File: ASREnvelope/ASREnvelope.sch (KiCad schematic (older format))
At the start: 47 parts

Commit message: add footprints
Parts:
- added J5: Ground, Connector_Wire:SolderWire-0.25sqmm_1x01_D0.65mm_OD2mm, symbol Connector:Conn_01x01_Female
- C1, C8: renamed from C?; footprint (none) -> Capacitor_THT:C_Disc_D3.0mm_W2.0mm_P2.50mm
- C2, C3: renamed from C?; footprint (none) -> Capacitor_THT:CP_Radial_D5.0mm_P2.00mm
- C4, C5, C6, C7: renamed from C?; footprint (none) -> Capacitor_THT:C_Rect_L10.3mm_W7.2mm_P7.50mm_MKS4
- D1, D2, D3, D4, D5, D6, D7, D8: renamed from D?; footprint (none) -> Diode_THT:D_DO-35_SOD27_P7.62mm_Horizontal
- J1, J2, J3, J4: renamed from J?; footprint (none) -> Connector_Wire:SolderWire-0.25sqmm_1x01_D0.65mm_OD2mm
- R1, R10, R11, R12, R13, R14, R15, R2, R3, R4, R5, R6, R7, R8, R9: renamed from R?; footprint (none) -> Resistor_THT:R_Axial_DIN0207_L6.3mm_D2.5mm_P7.62mm_Horizontal
- U1: renamed from U?; footprint (none) -> Package_DIP:DIP-14_W7.62mm_Socket
- U2: renamed from U?; footprint (none) -> Package_DIP:DIP-8_W7.62mm_Socket
- gave numbers to parts that had none: 4
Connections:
- net Earth: now also RV1.1, J5.1 (Pin_1); no longer RV1.3
- net at D5.1 (K): now also RV1.3; no longer RV1.1

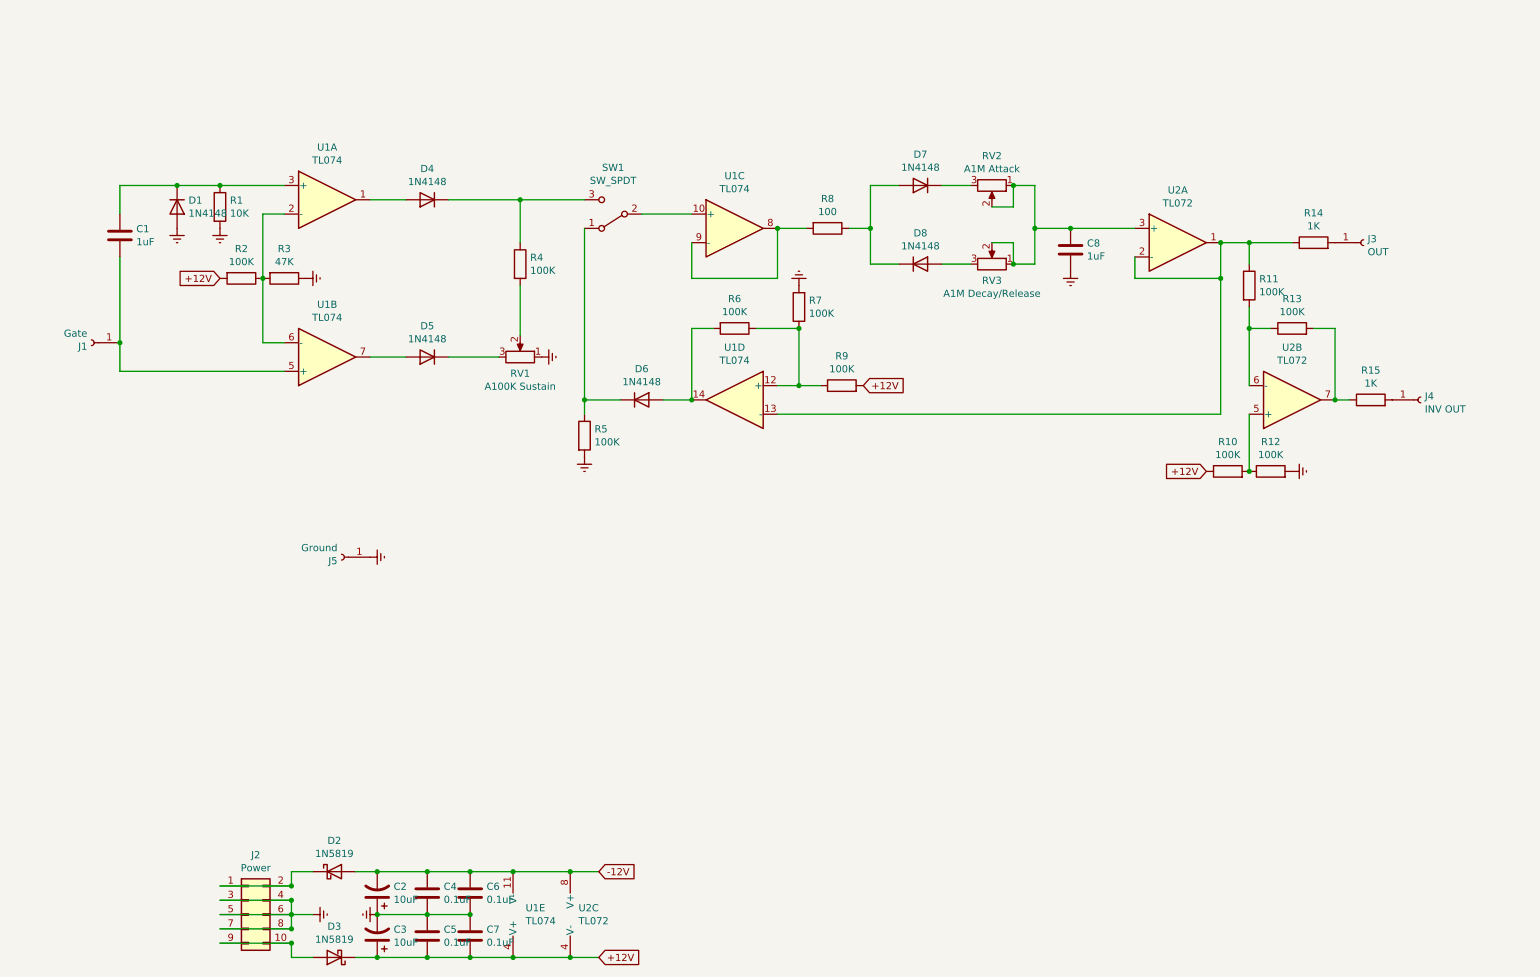
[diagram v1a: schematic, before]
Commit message: add through hole pot footprints
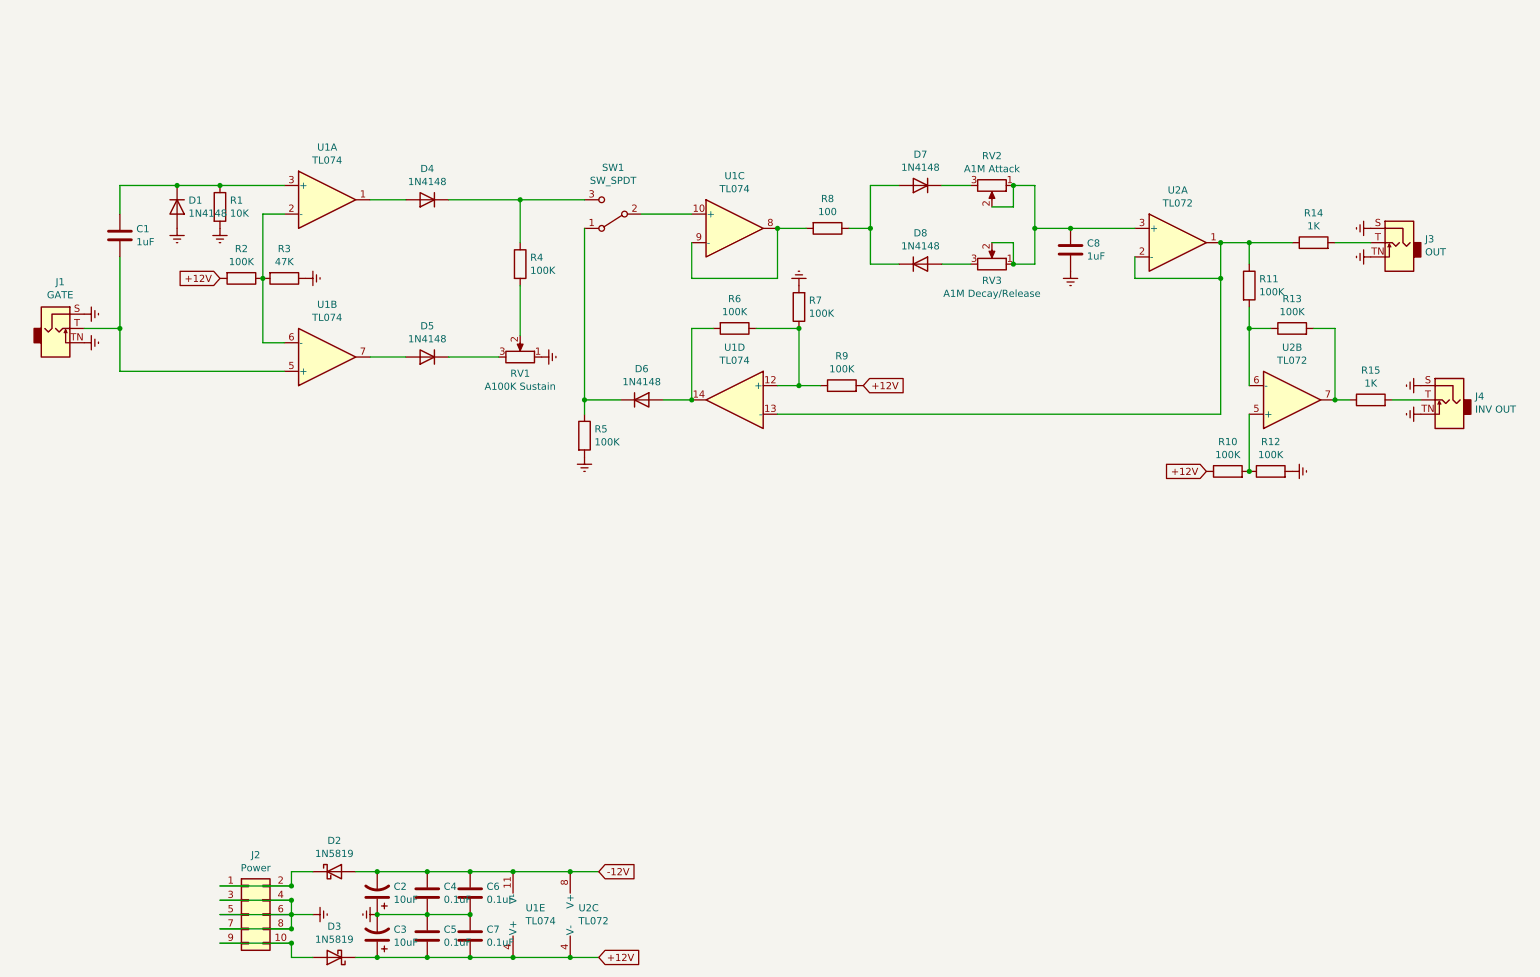
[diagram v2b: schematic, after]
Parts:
- removed J1: Gate, Connector_Wire:SolderWire-0.25sqmm_1x01_D0.65mm_OD2mm, symbol Connector:Conn_01x01_Female
- removed J3: OUT, Connector_Wire:SolderWire-0.25sqmm_1x01_D0.65mm_OD2mm, symbol Connector:Conn_01x01_Female
- removed J4: INV OUT, Connector_Wire:SolderWire-0.25sqmm_1x01_D0.65mm_OD2mm, symbol Connector:Conn_01x01_Female
- removed J5: Ground, Connector_Wire:SolderWire-0.25sqmm_1x01_D0.65mm_OD2mm, symbol Connector:Conn_01x01_Female
- added J1: GATE, Connector_Audio:Jack_3.5mm_QingPu_WQP-PJ398SM_Vertical_CircularHoles, symbol Connector:AudioJack2_SwitchT
- added J3: OUT, Connector_Audio:Jack_3.5mm_QingPu_WQP-PJ398SM_Vertical_CircularHoles, symbol Connector:AudioJack2_SwitchT
- added J4: INV OUT, Connector_Audio:Jack_3.5mm_QingPu_WQP-PJ398SM_Vertical_CircularHoles, symbol Connector:AudioJack2_SwitchT
- J2: footprint Connector_Wire:SolderWire-0.25sqmm_1x01_D0.65mm_OD2mm -> Connector_PinHeader_2.54mm:PinHeader_2x05_P2.54mm_Vertical
- RV1, RV2, RV3: footprint (none) -> Potentiometer_THT:Potentiometer_Alpha_RD901F-40-00D_Single_Vertical
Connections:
- net Earth: now also J1.S, J1.TN, J3.S, J3.TN, J4.S, J4.TN
- net at C1.2, U1.5 (+): now also J1.T
- net at R14.2: now also J3.T
- net at R15.2: now also J4.T
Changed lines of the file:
@@
 F 0 "J2" H 2300 7367 50  0000 C CNN
 F 1 "Power" H 2300 7276 50  0000 C CNN
-F 2 "Connector_Wire:SolderWire-0.25sqmm_1x01_D0.65mm_OD2mm" H 2250 6950 50  0001 C CNN
+F 2 "Connector_PinHeader_2.54mm:PinHeader_2x05_P2.54mm_Vertical" H 2250 6950 50  0001 C CNN
 F 3 "~" H 2250 6950 50  0001 C CNN
 	1    2250 6950
@@
 Wire Wire Line
 	3500 7250 3800 7250
-$Comp
-L Connector:Conn_01x01_Female J1
-U 1 1 62D5AD4C
-P 1150 2950
-F 0 "J1" H 1178 2976 50  0000 L CNN
-F 1 "Gate" H 1178 2885 50  0000 L CNN
-F 2 "Connector_Wire:SolderWire-0.25sqmm_1x01_D0.65mm_OD2mm" H 1150 2950 50  0001 C CNN
-F 3 "~" H 1150 2950 50  0001 C CNN
-	1    1150 2950
-	-1   0    0    1
-$EndComp
 Wire Wire Line
 	2500 2050 2350 2050
@@
 Wire Wire Line
 	2500 3150 1350 3150
-Wire Wire Line
-	1350 3150 1350 2950
 $Comp
 L Device:D D1
@@
 	1    0    0    -1
 $EndComp
-Wire Wire Line
-	1350 2950 1350 2350
-Connection ~ 1350 2950
 Wire Wire Line
 	1350 2050 1350 1850
@@
 F 0 "RV1" V 4035 3050 50  0000 C CNN
 F 1 "A100K Sustain" V 3944 3050 50  0000 C CNN
-F 2 "" H 4150 3050 50  0001 C CNN
+F 2 "Potentiometer_THT:Potentiometer_Alpha_RD901F-40-00D_Single_Vertical" H 4150 3050 50  0001 C CNN
 F 3 "~" H 4150 3050 50  0001 C CNN
 	1    4150 3050
@@
 F 0 "RV2" V 7243 1850 50  0000 C CNN
 F 1 "A1M Attack" V 7334 1850 50  0000 C CNN
-F 2 "" H 7450 1850 50  0001 C CNN
+F 2 "Potentiometer_THT:Potentiometer_Alpha_RD901F-40-00D_Single_Vertical" H 7450 1850 50  0001 C CNN
 F 3 "~" H 7450 1850 50  0001 C CNN
 	1    7450 1850
@@
 Connection ~ 9250 2250
 $Comp
-L Connector:Conn_01x01_Female J3
-U 1 1 62DDB569
-P 10050 2250
-F 0 "J3" H 10078 2276 50  0000 L CNN
-F 1 "OUT" H 10078 2185 50  0000 L CNN
-F 2 "Connector_Wire:SolderWire-0.25sqmm_1x01_D0.65mm_OD2mm" H 10050 2250 50  0001 C CNN
-F 3 "~" H 10050 2250 50  0001 C CNN
-	1    10050 2250
-	1    0    0    -1
-$EndComp
-$Comp
-L Connector:Conn_01x01_Female J4
-U 1 1 62DDE02F
-P 10450 3350
-F 0 "J4" H 10478 3376 50  0000 L CNN
-F 1 "INV OUT" H 10478 3285 50  0000 L CNN
-F 2 "Connector_Wire:SolderWire-0.25sqmm_1x01_D0.65mm_OD2mm" H 10450 3350 50  0001 C CNN
-F 3 "~" H 10450 3350 50  0001 C CNN
-	1    10450 3350
-	1    0    0    -1
-$EndComp
-$Comp
 L Device:R_POT RV3
 U 1 1 62DB3CBE
@@
 F 0 "RV3" V 7335 2400 50  0000 C CNN
 F 1 "A1M Decay/Release" V 7244 2400 50  0000 C CNN
-F 2 "" H 7450 2400 50  0001 C CNN
+F 2 "Potentiometer_THT:Potentiometer_Alpha_RD901F-40-00D_Single_Vertical" H 7450 2400 50  0001 C CNN
 F 3 "~" H 7450 2400 50  0001 C CNN
 	1    7450 2400
@@
 $EndComp
 $Comp
-L Connector:Conn_01x01_Female J5
-U 1 1 62CA67A4
-P 2900 4450
-F 0 "J5" H 2928 4476 50  0000 L CNN
-F 1 "Ground" H 2928 4385 50  0000 L CNN
-F 2 "Connector_Wire:SolderWire-0.25sqmm_1x01_D0.65mm_OD2mm" H 2900 4450 50  0001 C CNN
-F 3 "~" H 2900 4450 50  0001 C CNN
-	1    2900 4450
-	-1   0    0    1
-$EndComp
-$Comp
-L power:Earth #PWR0111
-U 1 1 62CA6B82
-P 3100 4450
-F 0 "#PWR0111" H 3100 4200 50  0001 C CNN
-F 1 "Earth" H 3100 4300 50  0001 C CNN
-F 2 "" H 3100 4450 50  0001 C CNN
-F 3 "~" H 3100 4450 50  0001 C CNN
-	1    3100 4450
-	0    -1   -1   0
+L Connector:AudioJack2_SwitchT J1
+U 1 1 62CBD424
+P 900 2850
+F 0 "J1" H 932 3175 50  0000 C CNN
+F 1 "GATE" H 932 3084 50  0000 C CNN
+F 2 "Connector_Audio:Jack_3.5mm_QingPu_WQP-PJ398SM_Vertical_CircularHoles" H 900 2850 50  0001 C CNN
+F 3 "~" H 900 2850 50  0001 C CNN
+	1    900  2850
+	1    0    0    -1
+$EndComp
+Wire Wire Line
+	1350 2350 1350 2850
+Wire Wire Line
+	1100 2850 1350 2850
+Connection ~ 1350 2850
+Wire Wire Line
+	1350 2850 1350 3150
+$Comp
+L power:Earth #PWR0112
+U 1 1 62CC2F54
+P 1100 2950
+F 0 "#PWR0112" H 1100 2700 50  0001 C CNN
+F 1 "Earth" H 1100 2800 50  0001 C CNN
+F 2 "" H 1100 2950 50  0001 C CNN
+F 3 "~" H 1100 2950 50  0001 C CNN
+	1    1100 2950
+	0    -1   -1   0
+$EndComp
+$Comp
+L power:Earth #PWR0113
+U 1 1 62CC34BA
+P 1100 2750
+F 0 "#PWR0113" H 1100 2500 50  0001 C CNN
+F 1 "Earth" H 1100 2600 50  0001 C CNN
+F 2 "" H 1100 2750 50  0001 C CNN
+F 3 "~" H 1100 2750 50  0001 C CNN
+	1    1100 2750
+	0    -1   -1   0
+$EndComp
+$Comp
+L Connector:AudioJack2_SwitchT J4
+U 1 1 62CC3778
+P 10650 3350
+F 0 "J4" H 10470 3375 50  0000 R CNN
+F 1 "INV OUT" H 10470 3284 50  0000 R CNN
+F 2 "Connector_Audio:Jack_3.5mm_QingPu_WQP-PJ398SM_Vertical_CircularHoles" H 10650 3350 50  0001 C CNN
+F 3 "~" H 10650 3350 50  0001 C CNN
+	1    10650 3350
+	-1   0    0    -1
+$EndComp
+$Comp
+L Connector:AudioJack2_SwitchT J3
+U 1 1 62CC766F
+P 10300 2250
+F 0 "J3" H 10120 2275 50  0000 R CNN
+F 1 "OUT" H 10120 2184 50  0000 R CNN
+F 2 "Connector_Audio:Jack_3.5mm_QingPu_WQP-PJ398SM_Vertical_CircularHoles" H 10300 2250 50  0001 C CNN
+F 3 "~" H 10300 2250 50  0001 C CNN
+	1    10300 2250
+	-1   0    0    -1
+$EndComp
+Wire Wire Line
+	10100 2250 9850 2250
+Wire Wire Line
+	10450 3350 10250 3350
+$Comp
+L power:Earth #PWR0114
+U 1 1 62CCD553
+P 10450 3450
+F 0 "#PWR0114" H 10450 3200 50  0001 C CNN
+F 1 "Earth" H 10450 3300 50  0001 C CNN
+F 2 "" H 10450 3450 50  0001 C CNN
+F 3 "~" H 10450 3450 50  0001 C CNN
+	1    10450 3450
+	0    1    1    0
+$EndComp
+$Comp
+L power:Earth #PWR0115
+U 1 1 62CCDE87
+P 10450 3250
+F 0 "#PWR0115" H 10450 3000 50  0001 C CNN
+F 1 "Earth" H 10450 3100 50  0001 C CNN
+F 2 "" H 10450 3250 50  0001 C CNN
+F 3 "~" H 10450 3250 50  0001 C CNN
+	1    10450 3250
+	0    1    1    0
+$EndComp
+$Comp
+L power:Earth #PWR0116
+U 1 1 62CCE0FD
+P 10100 2350
+F 0 "#PWR0116" H 10100 2100 50  0001 C CNN
+F 1 "Earth" H 10100 2200 50  0001 C CNN
+F 2 "" H 10100 2350 50  0001 C CNN
+F 3 "~" H 10100 2350 50  0001 C CNN
+	1    10100 2350
+	0    1    1    0
+$EndComp
+$Comp
+L power:Earth #PWR0117
+U 1 1 62CCE65D
+P 10100 2150
+F 0 "#PWR0117" H 10100 1900 50  0001 C CNN
+F 1 "Earth" H 10100 2000 50  0001 C CNN
+F 2 "" H 10100 2150 50  0001 C CNN
+F 3 "~" H 10100 2150 50  0001 C CNN
+	1    10100 2150
+	0    1    1    0
 $EndComp
 $EndSCHEMATC

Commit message: move circuit to two boards
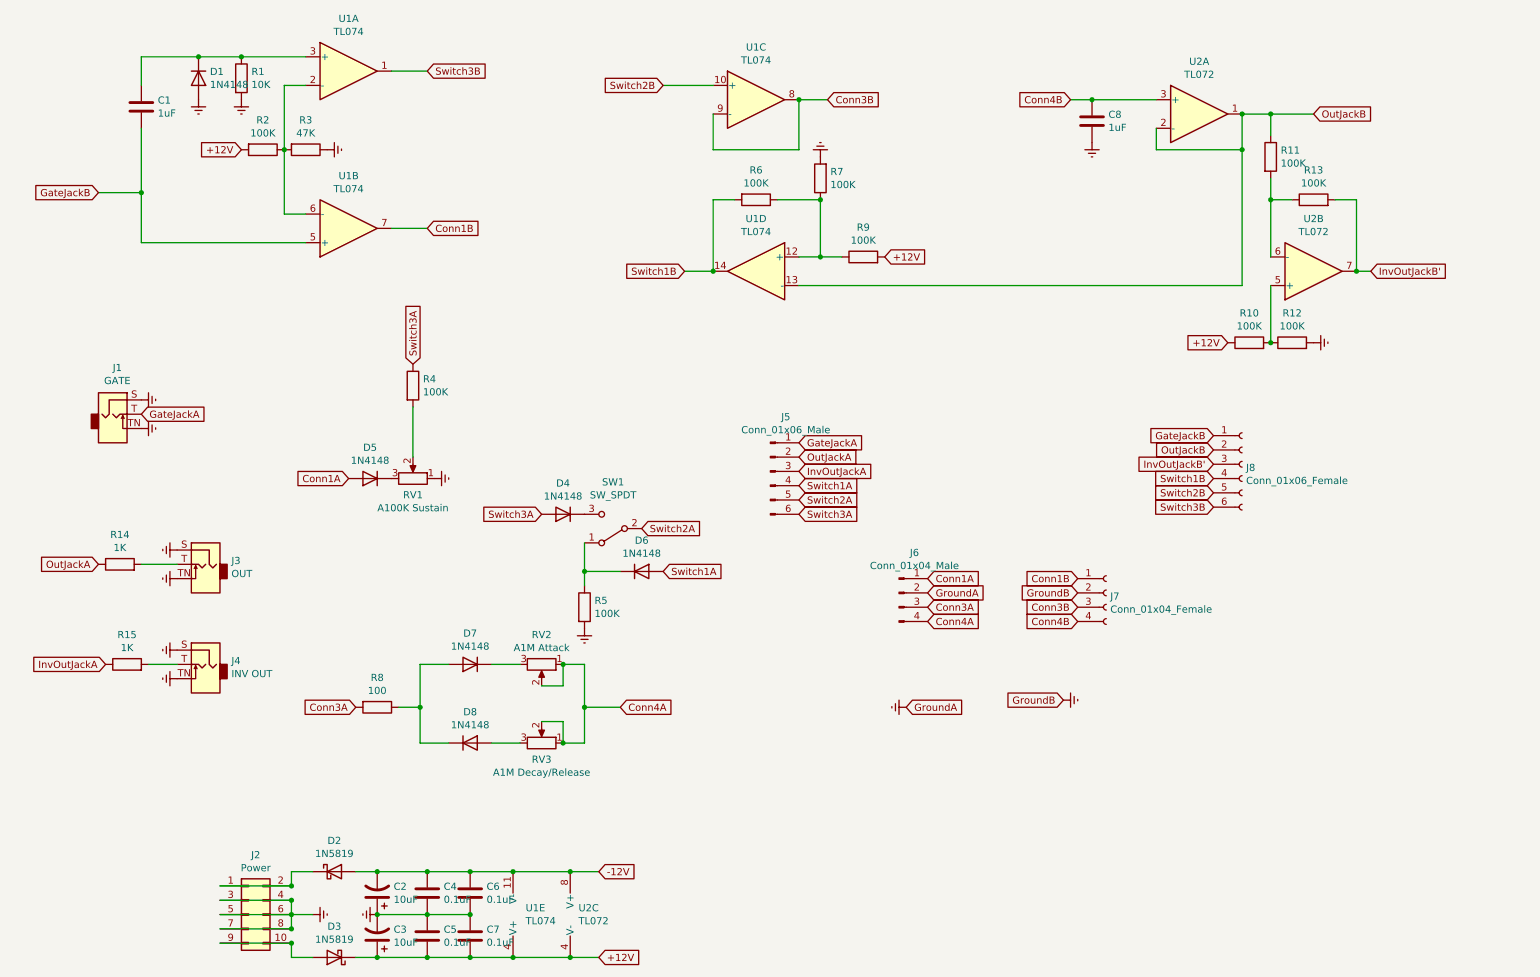
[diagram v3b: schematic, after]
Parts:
- added J5: Conn_01x06_Male, Connector_PinHeader_2.54mm:PinHeader_1x06_P2.54mm_Vertical, symbol Connector:Conn_01x06_Male
- added J6: Conn_01x04_Male, Connector_PinHeader_2.54mm:PinHeader_1x04_P2.54mm_Vertical, symbol Connector:Conn_01x04_Male
- added J7: Conn_01x04_Female, Connector_PinHeader_2.54mm:PinHeader_1x04_P2.54mm_Vertical, symbol Connector:Conn_01x04_Female
- added J8: Conn_01x06_Female, Connector_PinHeader_2.54mm:PinHeader_1x06_P2.54mm_Vertical, symbol Connector:Conn_01x06_Female
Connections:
- net Earth: now also J6.2 (Pin_2), J7.2 (Pin_2)
- net GateJackB: now reaches C1.2, U1.5 (+)
- net GateJackB: now also J8.1 (Pin_1); no longer J1.T
- net Switch3A: now reaches D4.2 (A)
- net Switch3A: now also R4.1, J5.6 (Pin_6); no longer U1.1
- net Conn1A: now reaches D5.2 (A)
- net Conn1A: now also J6.1 (Pin_1); no longer U1.7
- net Switch2A: now reaches SW1.2 (B)
- net Switch2A: now also J5.5 (Pin_5); no longer U1.10 (+)
- net Conn3B: now reaches U1.8, U1.9 (-)
- net Conn3B: now also J7.3 (Pin_3); no longer R8.2
- net OutJackB: now reaches R11.1, U1.13 (-), U2.1, U2.2 (-)
- net OutJackB: now also J8.2 (Pin_2); no longer R14.1
- net Switch1B: now reaches R6.2, U1.14
- net Switch1B: now also J8.4 (Pin_4); no longer D6.2 (A)
- net InvOutJackB': now reaches R13.2, U2.7
- net InvOutJackB': now also J8.3 (Pin_3); no longer R15.1
- net Conn4A: now reaches RV2.1, RV2.2, RV3.1, RV3.2
- net Conn4A: now also J6.4 (Pin_4); no longer C8.1, U2.3 (+)
- net at D4.1 (K), SW1.3 (C): no longer R4.1
- new net Conn1B: J7.1 (Pin_1), U1.7
- new net Conn3A: J6.3 (Pin_3), R8.2
- new net Conn4B: C8.1, J7.4 (Pin_4), U2.3 (+)
- new net GateJackA: J1.T, J5.1 (Pin_1)
- new net InvOutJackA: J5.3 (Pin_3), R15.1
- new net OutJackA: J5.2 (Pin_2), R14.1
- new net Switch1A: D6.2 (A), J5.4 (Pin_4)
- new net Switch2B: J8.5 (Pin_5), U1.10 (+)
- new net Switch3B: J8.6 (Pin_6), U1.1
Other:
- moved on the sheet: C1, C8, D1, D4, D5, D6, D7, D8, J1, J3, J4, R1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
